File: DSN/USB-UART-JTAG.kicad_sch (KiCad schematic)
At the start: 88 parts

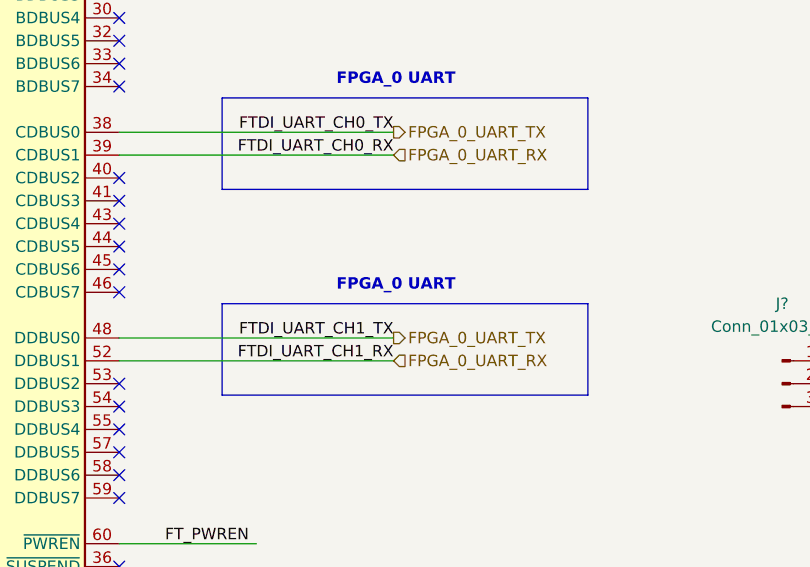
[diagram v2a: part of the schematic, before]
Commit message: Added Footprints
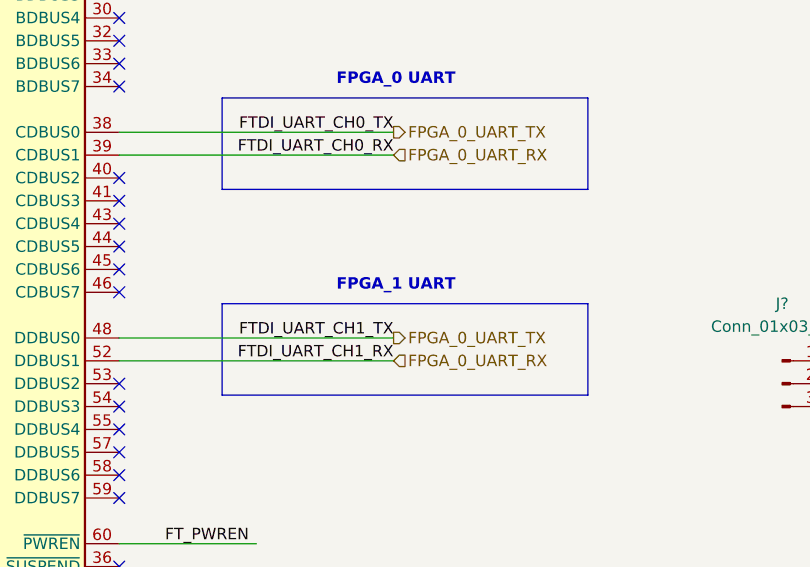
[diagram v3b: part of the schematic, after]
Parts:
- removed R?: 0R, Resistor_SMD:R_0402_1005Metric, symbol Device:R_US
- removed U?: ADG794, symbol Analog:ADG794
- added R?: 0R, Resistor_SMD:R_0402_1005Metric, symbol Device:R_US
- added U?: ADG794, Package_SO:QSOP-16_3.9x4.9mm_P0.635mm, symbol Analog:ADG794
- U?: footprint (none) -> Package_TO_SOT_SMD:SOT-23-6; MFR PN (none) -> 93LC56B
- U?: footprint (none) -> Package_SO:QSOP-16_3.9x4.9mm_P0.635mm; MFR PN (none) -> ADG794BRQZ
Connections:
- net +3V3_VCCIO: now also R?.2, U?.15 (S4A), U?.16 (VDD)
- net FPGA_0_TCK: now also U?.4 (D1)
- net FPGA_0_TDI: now also U?.7 (D2)
- net FPGA_0_TDO: now also U?.9 (D3)
- net FPGA_0_TMS: now also U?.12 (D4)
- net FTDI_TCK_CH0: now also U?.2 (S1A)
- net FTDI_TDI_CH0: now also U?.5 (S2A)
- net FTDI_TDO_CH0: now also U?.11 (S3A)
- net FTDI_TMS_CH0: now also U?.15 (S4A)
- net GND: now also U?.8 (GND)
- net JTAG_H_CH0_TCK: now also U?.3 (S1B)
- net JTAG_H_CH0_TDI: now also U?.6 (S2B)
- net JTAG_H_CH0_TDO: now also U?.10 (S3B)
- net JTAG_H_CH0_TMS: now also U?.13 (S4B)
- net USB_3V3_AUX: now also R?.1
- net at J?.2 (Pin_2): now also U?.1 (IN)
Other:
- note added: "FPGA_1 UART"
- title: (none) -> FT4232 JTAG & UART
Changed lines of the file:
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@@
 (kicad_sch (version 20211123) (generator eeschema)
   (paper "A2")
+  (title_block
+    (title "FT4232 JTAG & UART")
+    (date "2023-03-07")
+    (rev "A")
+    (comment 1 "Designed by DragonEnjoyer :3")
+  )
   (junction (at 304.8 182.88) (diameter 0) (color 0 0 0 0)
   )
@@
     (effects (font (size 1.27 1.27)) (justify left bottom))
   )
-  (text "FPGA_0 UART" (at 349.25 255.27 0)
+  (text "FPGA_1 UART" (at 349.25 255.27 0)
     (effects (font (size 1.27 1.27) (thickness 0.254) bold) (justify left bottom))
   )
@@
     (pin "2")
   )
-  (symbol (lib_id "Analog:ADG794") (at 444.5 203.2 0) (unit 1)
-    (in_bom yes) (on_board yes) (fields_autoplaced)
-    (property "Reference" "U?" (id 0) (at 454.025 163.83 0))
-    (property "Value" "ADG794" (id 1) (at 454.025 166.37 0))
-    (property "Footprint" "" (id 2) (at 415.29 182.88 0)
-      (effects (font (size 1.27 1.27)) hide)
-    )
-    (property "Datasheet" "" (id 3) (at 415.29 182.88 0)
-      (effects (font (size 1.27 1.27)) hide)
-    )
-    (pin "1")
-    (pin "10")
-    (pin "11")
-    (pin "12")
-    (pin "13")
-    (pin "15")
-    (pin "15")
-    (pin "16")
-    (pin "2")
-    (pin "3")
-    (pin "4")
-    (pin "5")
-    (pin "6")
-    (pin "7")
-    (pin "8")
-    (pin "9")
-  )
   (symbol (lib_id "Device:R_US") (at 111.76 104.14 90) (mirror x) (unit 1)
     (in_bom yes) (on_board yes)
@@
     (pin "2")
   )
+  (symbol (lib_id "Analog:ADG794") (at 444.5 203.2 0) (unit 1)
+    (in_bom yes) (on_board yes) (fields_autoplaced)
+    (property "Reference" "U?" (id 0) (at 454.025 163.83 0))
+    (property "Value" "ADG794" (id 1) (at 454.025 166.37 0))
+    (property "Footprint" "Package_SO:QSOP-16_3.9x4.9mm_P0.635mm" (id 2) (at 415.29 182.88 0)
+      (effects (font (size 1.27 1.27)) hide)
+    )
+    (property "Datasheet" "https://www.analog.com/media/en/technical-documentation/data-sheets/ADG794.pdf" (id 3) (at 415.29 182.88 0)
+      (effects (font (size 1.27 1.27)) hide)
+    )
+    (property "MFR PN" "ADG794BRQZ" (id 4) (at 444.5 203.2 0)
+      (effects (font (size 1.27 1.27)) hide)
+    )
+    (pin "1")
+    (pin "10")
+    (pin "11")
+    (pin "12")
+    (pin "13")
+    (pin "15")
+    (pin "15")
+    (pin "16")
+    (pin "2")
+    (pin "3")
+    (pin "4")
+    (pin "5")
+    (pin "6")
+    (pin "7")
+    (pin "8")
+    (pin "9")
+  )
   (symbol (lib_id "power:GND") (at 99.06 300.99 0) (unit 1)
     (in_bom yes) (on_board yes)
@@
       (effects (font (size 1.27 1.27)) (justify left))
     )
-    (property "Footprint" "" (id 2) (at 86.36 254 0)
+    (property "Footprint" "Package_TO_SOT_SMD:SOT-23-6" (id 2) (at 86.36 254 0)
       (effects (font (size 1.27 1.27)) hide)
     )
@@
       (effects (font (size 1.27 1.27)) hide)
     )
+    (property "MFR PN" "93LC56B" (id 4) (at 86.36 254 0)
+      (effects (font (size 1.27 1.27)) hide)
+    )
     (pin "1")
     (pin "2")
@@
     (property "Reference" "U?" (id 0) (at 454.025 250.19 0))
     (property "Value" "ADG794" (id 1) (at 454.025 252.73 0))
-    (property "Footprint" "" (id 2) (at 415.29 269.24 0)
+    (property "Footprint" "Package_SO:QSOP-16_3.9x4.9mm_P0.635mm" (id 2) (at 415.29 269.24 0)
       (effects (font (size 1.27 1.27)) hide)
     )
-    (property "Datasheet" "" (id 3) (at 415.29 269.24 0)
+    (property "Datasheet" "https://www.analog.com/media/en/technical-documentation/data-sheets/ADG794.pdf" (id 3) (at 415.29 269.24 0)
+      (effects (font (size 1.27 1.27)) hide)
+    )
+    (property "MFR PN" "ADG794BRQZ" (id 4) (at 444.5 289.56 0)
       (effects (font (size 1.27 1.27)) hide)
     )
@@
     (pin "1")
   )
+  (symbol (lib_id "Device:R_US") (at 116.84 209.55 90) (unit 1)
+    (in_bom yes) (on_board yes) (fields_autoplaced)
+    (property "Reference" "R?" (id 0) (at 116.84 203.2 90))
+    (property "Value" "0R" (id 1) (at 116.84 205.74 90))
+    (property "Footprint" "Resistor_SMD:R_0402_1005Metric" (id 2) (at 117.094 208.534 90)
+      (effects (font (size 1.27 1.27)) hide)
+    )
+    (property "Datasheet" "https://www.mouser.com/datasheet/2/447/PYu_RC_Group_51_RoHS_L_11-1984063.pdf" (id 3) (at 116.84 209.55 0)
+      (effects (font (size 1.27 1.27)) hide)
+    )
+    (property "MRF PN" "RC0402FR-070RL" (id 4) (at 116.84 209.55 90)
+      (effects (font (size 1.27 1.27)) hide)
+    )
+    (pin "1")
+    (pin "2")
+  )
   (symbol (lib_id "Device:R_US") (at 392.43 55.88 0) (mirror y) (unit 1)
     (in_bom yes) (on_board yes)
@@
     (pin "1")
   )
-  (symbol (lib_id "Device:R_US") (at 116.84 209.55 90) (unit 1)
-    (in_bom yes) (on_board yes) (fields_autoplaced)
-    (property "Reference" "R?" (id 0) (at 116.84 203.2 90))
-    (property "Value" "0R" (id 1) (at 116.84 205.74 90))
-    (property "Footprint" "Resistor_SMD:R_0402_1005Metric" (id 2) (at 117.094 208.534 90)
-      (effects (font (size 1.27 1.27)) hide)
-    )
-    (property "Datasheet" "~" (id 3) (at 116.84 209.55 0)
-      (effects (font (size 1.27 1.27)) hide)
-    )
-    (property "MRF PN" "RC0402FR-070RL" (id 4) (at 116.84 209.55 90)
-      (effects (font (size 1.27 1.27)) hide)
-    )
-    (pin "1")
-    (pin "2")
-  )
   (symbol (lib_id "Device:C_Small") (at 306.07 147.32 0) (unit 1)

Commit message: Added component ref des
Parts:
- gave numbers to parts that had none: 88
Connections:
- net FPGA_0_TCK: no longer R183.2, U19.4 (D1)
- net FPGA_0_TDI: no longer R185.2, U19.7 (D2)
- net FPGA_0_TDO: no longer R187.2, U19.9 (D3)
- net FPGA_0_TMS: no longer R189.2, U19.12 (D4)
- net FPGA_0_UART_RX: no longer U17.52 (DDBUS1)
- net FPGA_0_UART_TX: no longer U17.48 (DDBUS0)
- new net FPGA_1_TCK: R183.2, U19.4 (D1)
- new net FPGA_1_TDI: R185.2, U19.7 (D2)
- new net FPGA_1_TDO: R187.2, U19.9 (D3)
- new net FPGA_1_TMS: R189.2, U19.12 (D4)
- new net FPGA_1_UART_RX: U17.52 (DDBUS1)
- new net FPGA_1_UART_TX: U17.48 (DDBUS0)

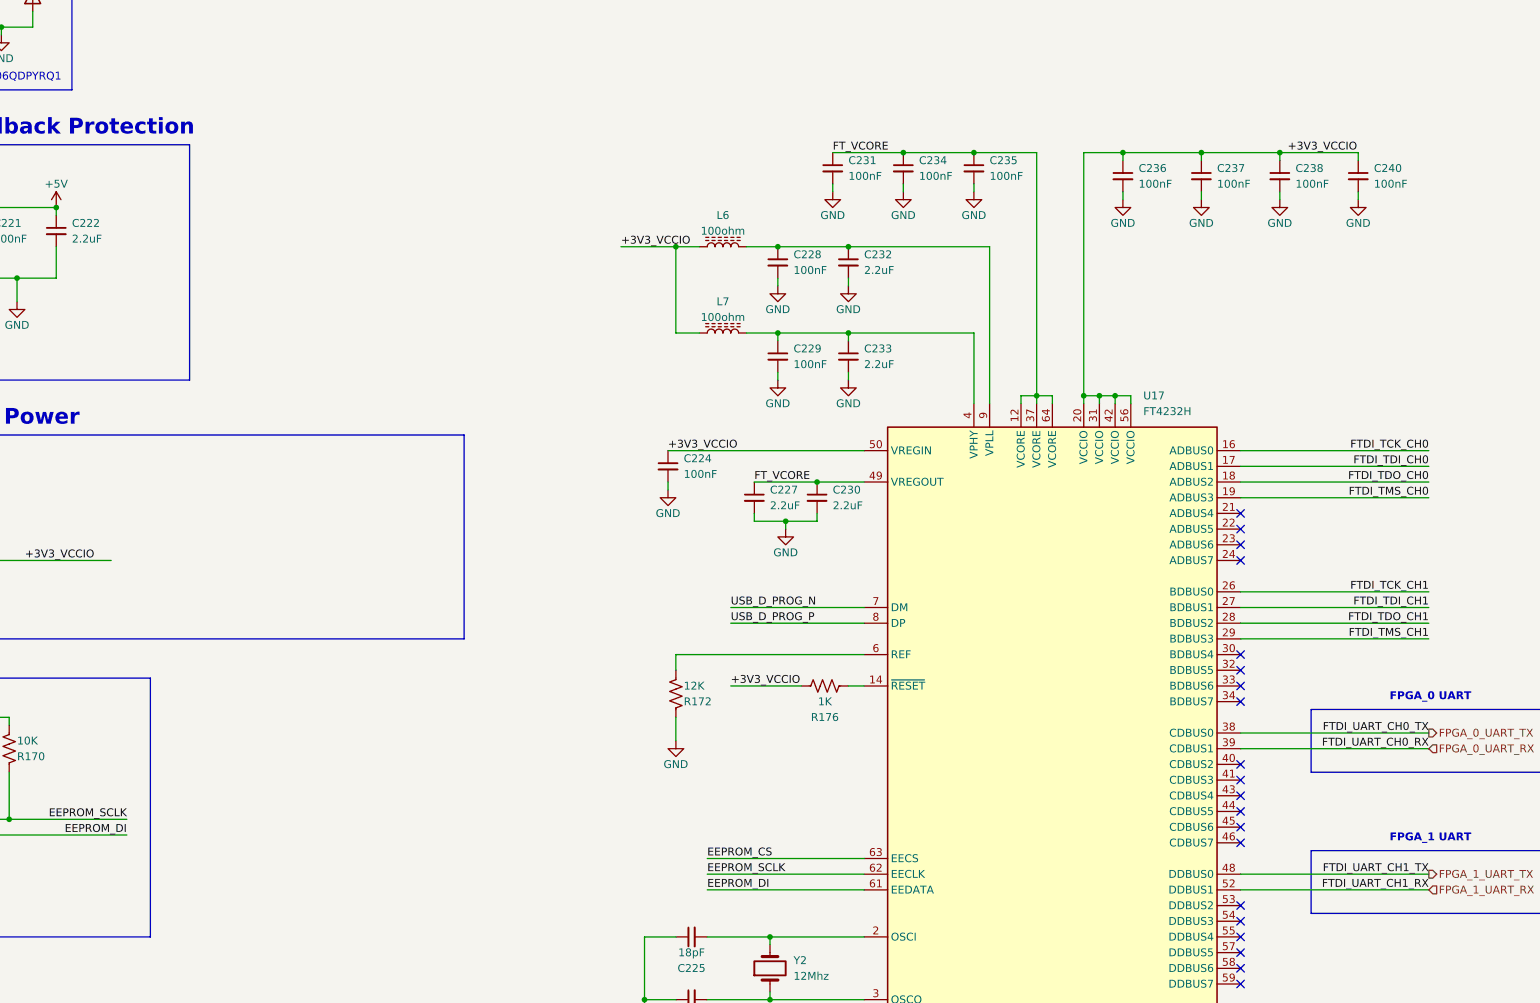
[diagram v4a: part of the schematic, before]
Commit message: Fixed all ERC Errors
Warnings can be ignored
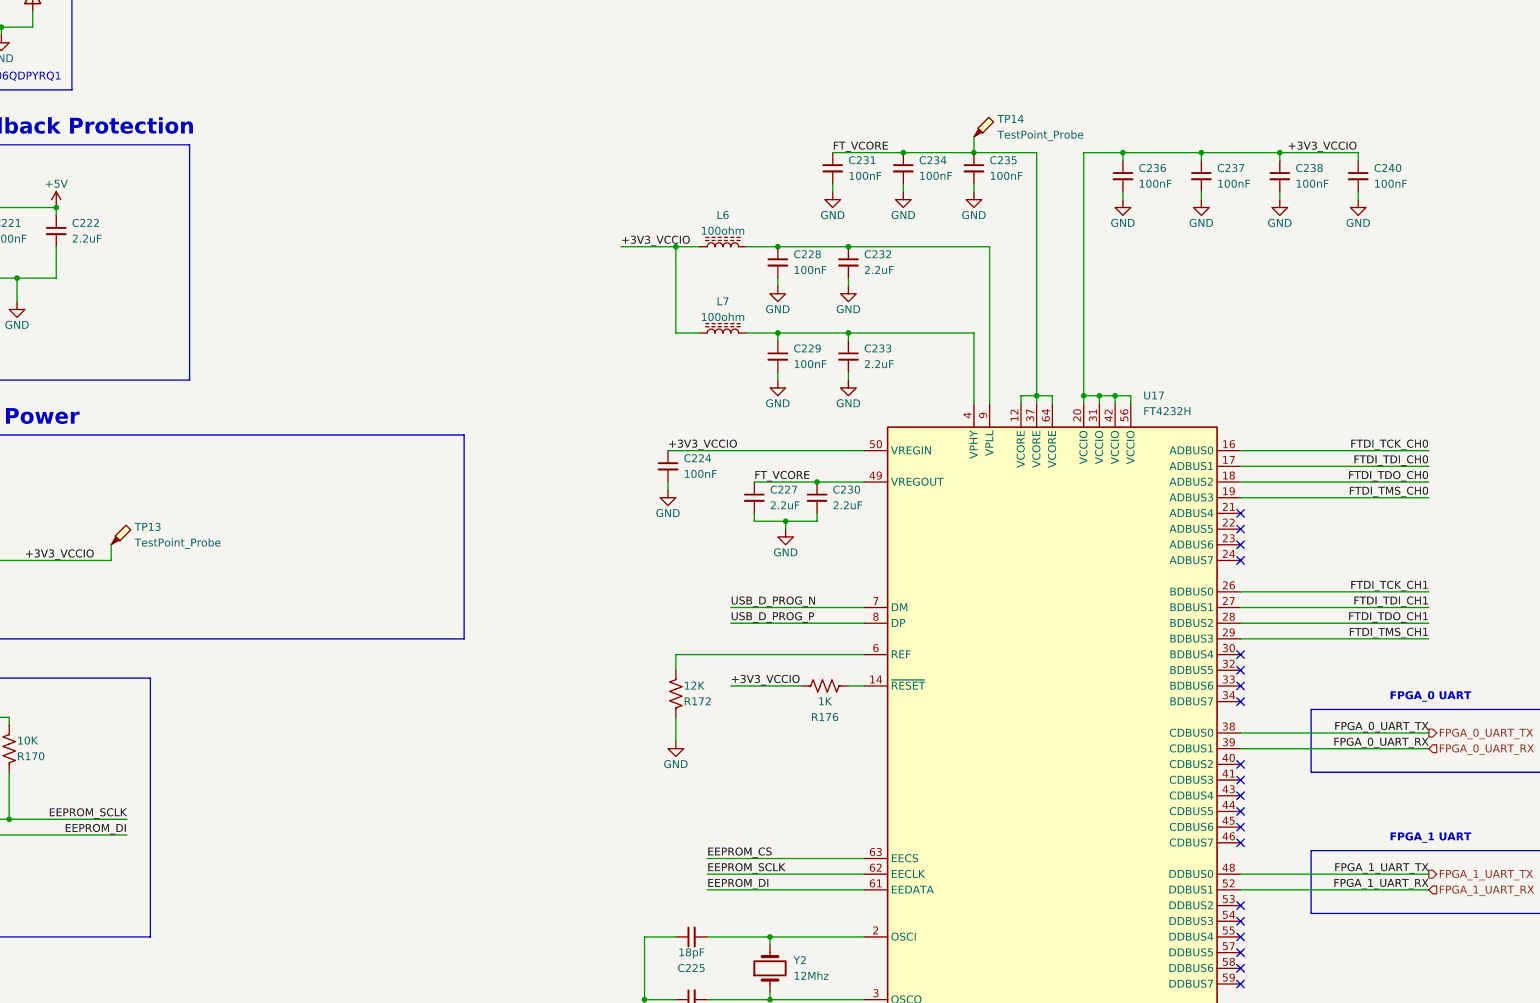
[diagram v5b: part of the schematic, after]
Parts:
- added TP13, TP14: TestPoint_Probe, TestPoint:TestPoint_Loop_D2.50mm_Drill1.85mm, symbol Connector:TestPoint_Probe
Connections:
- net +3V3_VCCIO: now also TP13.1
- net FT_VCORE: now also TP14.1
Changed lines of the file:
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@@
     (stroke (width 0) (type default) (color 0 0 0 0))
   )
+  (wire (pts (xy 281.94 140.97) (xy 281.94 143.51))
+    (stroke (width 0) (type default) (color 0 0 0 0))
+  )
   (wire (pts (xy 99.06 162.56) (xy 86.36 162.56))
     (stroke (width 0) (type default) (color 0 0 0 0))
@@
     (stroke (width 0) (type default) (color 0 0 0 0))
   )
+  (wire (pts (xy 142.24 207.01) (xy 142.24 209.55))
+    (stroke (width 0) (type default) (color 0 0 0 0))
+  )
   (wire (pts (xy 444.5 173.99) (xy 441.96 173.99))
     (stroke (width 0) (type default) (color 0 0 0 0))
@@
     (effects (font (size 1.27 1.27)) (justify left bottom))
   )
-  (label "FTDI_UART_CH0_RX" (at 355.6 240.03 180)
+  (label "FPGA_0_UART_RX" (at 355.6 240.03 180)
     (effects (font (size 1.27 1.27)) (justify right bottom))
   )
@@
     (effects (font (size 1.27 1.27)) (justify left bottom))
   )
-  (label "FTDI_UART_CH0_TX" (at 355.6 237.49 180)
+  (label "FPGA_0_UART_TX" (at 355.6 237.49 180)
     (effects (font (size 1.27 1.27)) (justify right bottom))
   )
@@
     (effects (font (size 1.27 1.27)) (justify left bottom))
   )
-  (label "FTDI_UART_CH1_TX" (at 355.6 260.35 180)
+  (label "FPGA_1_UART_TX" (at 355.6 260.35 180)
     (effects (font (size 1.27 1.27)) (justify right bottom))
   )
@@
     (effects (font (size 1.27 1.27)) (justify right bottom))
   )
-  (label "FTDI_UART_CH1_RX" (at 355.6 262.89 180)
+  (label "FPGA_1_UART_RX" (at 355.6 262.89 180)
     (effects (font (size 1.27 1.27)) (justify right bottom))
   )
@@
     (pin "1")
   )
+  (symbol (lib_id "Connector:TestPoint_Probe") (at 281.94 140.97 0) (unit 1)
+    (in_bom yes) (on_board yes)
+    (property "Reference" "TP14" (id 0) (at 285.75 138.1124 0)
+      (effects (font (size 1.27 1.27)) (justify left))
+    )
+    (property "Value" "TestPoint_Probe" (id 1) (at 285.75 140.6524 0)
+      (effects (font (size 1.27 1.27)) (justify left))
+    )
+    (property "Footprint" "TestPoint:TestPoint_Loop_D2.50mm_Drill1.85mm" (id 2) (at 287.02 140.97 0)
+      (effects (font (size 1.27 1.27)) hide)
+    )
+    (property "Datasheet" "~" (id 3) (at 287.02 140.97 0)
+      (effects (font (size 1.27 1.27)) hide)
+    )
+    (pin "1")
+  )
   (symbol (lib_id "Device:R_US") (at 110.49 240.03 0) (mirror y) (unit 1)
     (in_bom yes) (on_board yes)
@@
       (effects (font (size 1.27 1.27)) hide)
     )
+    (pin "1")
+  )
+  (symbol (lib_id "Connector:TestPoint_Probe") (at 142.24 207.01 0) (unit 1)
+    (in_bom yes) (on_board yes)
+    (property "Reference" "TP13" (id 0) (at 146.05 204.1524 0)
+      (effects (font (size 1.27 1.27)) (justify left))
+    )
+    (property "Value" "TestPoint_Probe" (id 1) (at 146.05 206.6924 0)
+      (effects (font (size 1.27 1.27)) (justify left))
+    )
+    (property "Footprint" "TestPoint:TestPoint_Loop_D2.50mm_Drill1.85mm" (id 2) (at 147.32 207.01 0)
+      (effects (font (size 1.27 1.27)) hide)
+    )
+    (property "Datasheet" "~" (id 3) (at 147.32 207.01 0)
+      (effects (font (size 1.27 1.27)) hide)
+    )

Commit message: Initial PCB Layout
Initial layout and part placement
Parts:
- J28, J31: footprint (none) -> Connector_PinHeader_2.54mm:PinHeader_2x07_P2.54mm_Vertical
- J29, J30: footprint (none) -> Connector_PinHeader_2.54mm:PinHeader_1x03_P2.54mm_Vertical
- U15: footprint Package_TO_SOT_SMD:SOT-23-6 -> Package_SO:SOIC-8_3.9x4.9mm_P1.27mm

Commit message: Updated Layout
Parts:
- removed D37: BZV55B5V6, Diode_SMD:D_MiniMELF, symbol Diode:BZV55B5V6
- removed Y2: 12Mhz, Crystal:Crystal_SMD_ECS_CSM3X-2Pin_7.6x4.1mm, symbol Device:Crystal
- added D37: 5.6V Zener, Diode_SMD:D_SOD-123, symbol Device:D_Zener
- added TP17: TestPoint_Probe, TestPoint:TestPoint_Loop_D1.80mm_Drill1.0mm_Beaded, symbol Connector:TestPoint_Probe
- added Y3: Crystal_GND24, Crystal:Crystal_SMD_3225-4Pin_3.2x2.5mm, symbol Device:Crystal_GND24
- TP13, TP14: footprint TestPoint:TestPoint_Loop_D2.50mm_Drill1.85mm -> TestPoint:TestPoint_Loop_D1.80mm_Drill1.0mm_Beaded
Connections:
- net +3V3_VCCIO: now also TP14.1; no longer TP13.1
- net +5V: now also D37.1 (K)
- net FT_VCORE: now also TP17.1; no longer TP14.1
- net GND: now also Y3.2, Y3.4
- net VBUS_AUX_PROG: now also TP13.1
- net at Q21.4 (G), R161.1: now also D37.2 (A)
- net at C226.2, U17.3 (OSCO): now also Y3.1
- net at C225.2, U17.2 (OSCI): now also Y3.3
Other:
- moved on the sheet: C226
